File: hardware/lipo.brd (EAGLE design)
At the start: 33.5 x 34.6 mm, 62 parts, among them IC1 4066D, IC2 4066D, J1 MICRO_USB_B_HIROSE_ZX62-B-5PA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, Q1 IRLML6402, SW1 TVAF06-A020B-R, U1 LT6106CS5#PBF, U2 NJM12888F, U3 MCP73831, U5 TCK106AF,LF, X1 FA-238

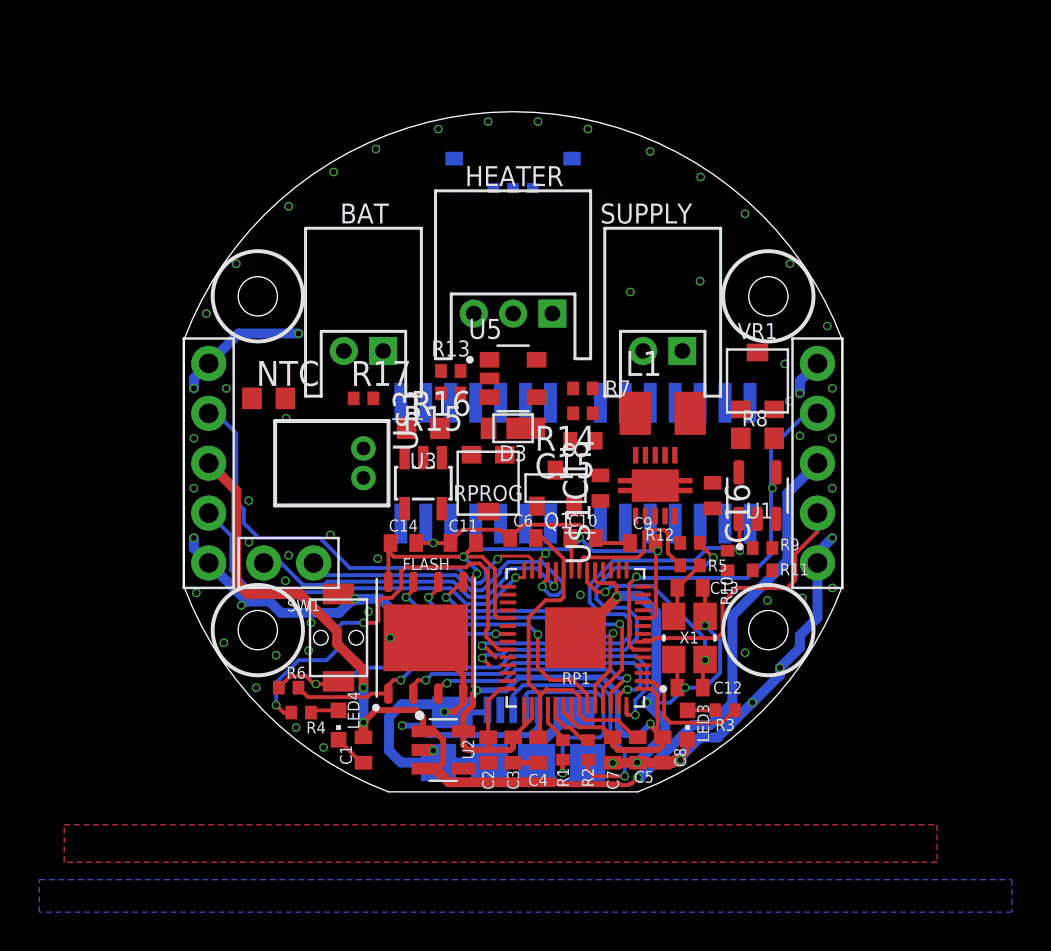
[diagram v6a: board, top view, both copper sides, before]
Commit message: LiPoモジュールの基板設計です。
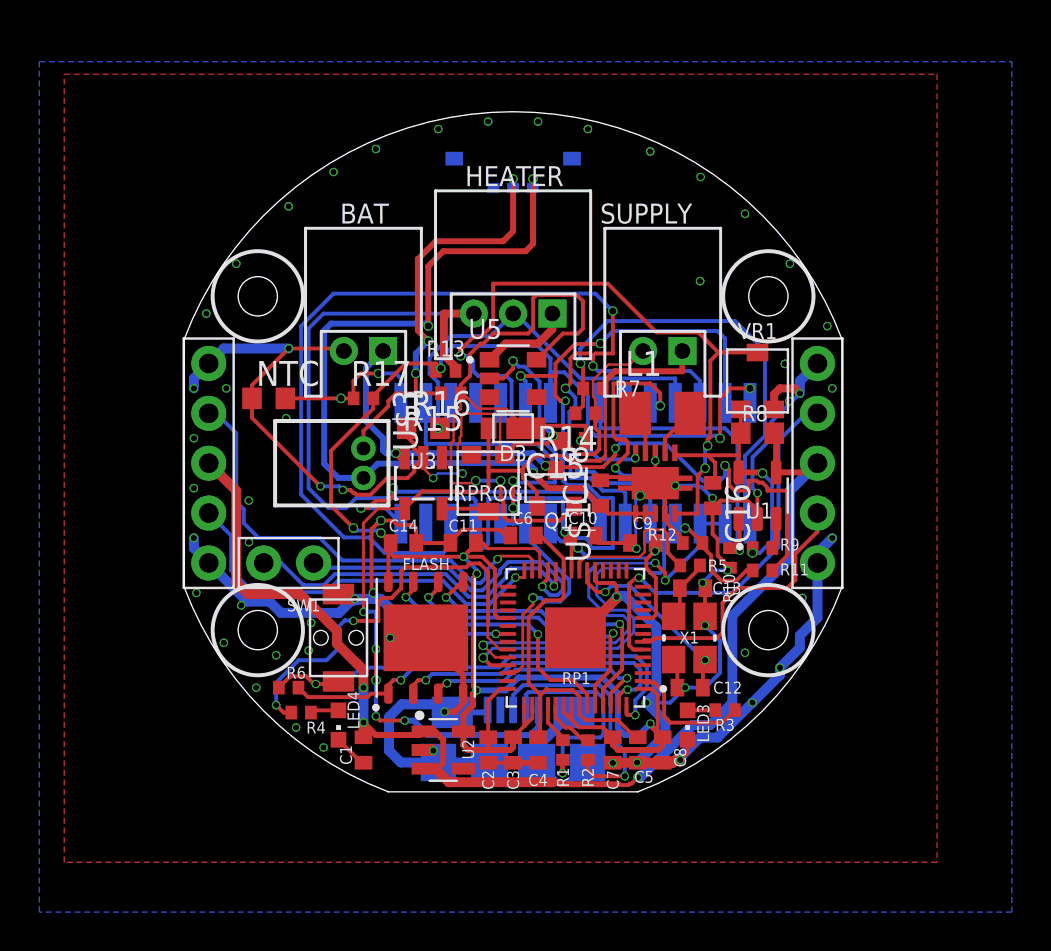
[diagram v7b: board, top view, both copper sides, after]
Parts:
- moved C15 0.51 mm to (3.05, 1.14)
- moved R7 0.51 mm to (4.06, 3.81)
- moved C18 0.25 mm to (4.45, -1.52)
- moved R13 0.25 mm to (-3.43, 4.70)
- moved R8 0.25 mm to (12.4, 1.52)
- moved R10 0.18 mm to (11.0, -4.83)
- moved C13 0.13 mm to (9.14, -6.36)
- moved R12 0.13 mm to (9.14, -4.06)
- moved C10 0.13 mm to (3.56, -3.68)
- moved C6 0.13 mm to (0.51, -3.68)
- moved U$1 0.13 mm to (7.24, -1.02)
- moved R14 0.13 mm to (3.68, 2.54)
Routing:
- net GND: track 119.6 -> 212.1 mm, vias 64 -> 69
- net ADC_SEL2: track 0.00 -> 59.8 mm, vias 0 -> 3
- net V+_V: track 0.00 -> 48.9 mm, vias 0 -> 3
- net VDD: track 74.1 -> 122.3 mm, vias 7 -> 12
- net EN: track 0.00 -> 43.7 mm, vias 0 -> 3
- net VPP: track 8.19 -> 49.9 mm, vias 3 -> 5
- net N$3: track 0.00 -> 39.5 mm, vias 0 -> 4
- net VBAT: track 0.00 -> 35.7 mm, vias 0 -> 4
- net ADC1_IN: track 0.00 -> 35.1 mm, vias 0 -> 3
- net TEMP: track 0.00 -> 31.9 mm
- net ADC_SEL1: track 0.00 -> 27.1 mm, vias 0 -> 3
- net ADC2_IN: track 0.00 -> 26.9 mm, vias 0 -> 3
- net SUPPLY_V: track 0.00 -> 23.4 mm, vias 0 -> 1
- net ADC0_IN: track 0.00 -> 23.1 mm, vias 0 -> 3
- net N$14: track 0.00 -> 21.7 mm, vias 0 -> 3
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
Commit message: 回路微修正
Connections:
- removed net N$5: J1.ID
- removed net VSS: IC1.7, IC2.7
- net ADC_SEL1: now also RP1.16
- net ADC_SEL2: now also RP1.31
- net ADC_SEL3: now also RP1.29
- net CHARGE: now also RP1.18
- net GND: now also IC1.7, IC2.7
- net HEATER: now also RP1.17
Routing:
- net VSS: track 16.4 -> 0.00 mm, vias 2 -> 0
- net ADC_SEL3: track 0.00 -> 16.2 mm, vias 0 -> 1
- net HEATER: track 0.00 -> 14.1 mm, vias 0 -> 2
- net CHARGE: track 0.00 -> 13.2 mm, vias 0 -> 4
- net ADC_SEL2: track 59.8 -> 69.9 mm, vias 3 -> 6
- net GND: track 212.1 -> 216.9 mm, vias 69 -> 71
- net V+_V: track 48.9 -> 44.1 mm
- net ADC_SEL1: track 27.1 -> 28.9 mm, vias 3 -> 4
- net ADC2_IN: track 26.9 -> 28.2 mm
- net LED1: track 21.9 -> 23.2 mm
- net ADC1_IN: track 35.1 -> 34.2 mm
- net VPP: track 49.9 -> 50.7 mm
- net XOUT1: track 8.19 -> 9.01 mm
- net SWCLK: track 18.0 -> 17.2 mm
- net SWD: track 17.1 -> 16.4 mm
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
